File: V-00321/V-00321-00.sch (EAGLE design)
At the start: 3 parts, among them X1 D-SUB9-SAMICE, X2 Lumberg-Lu12MP, X3 LE4MP

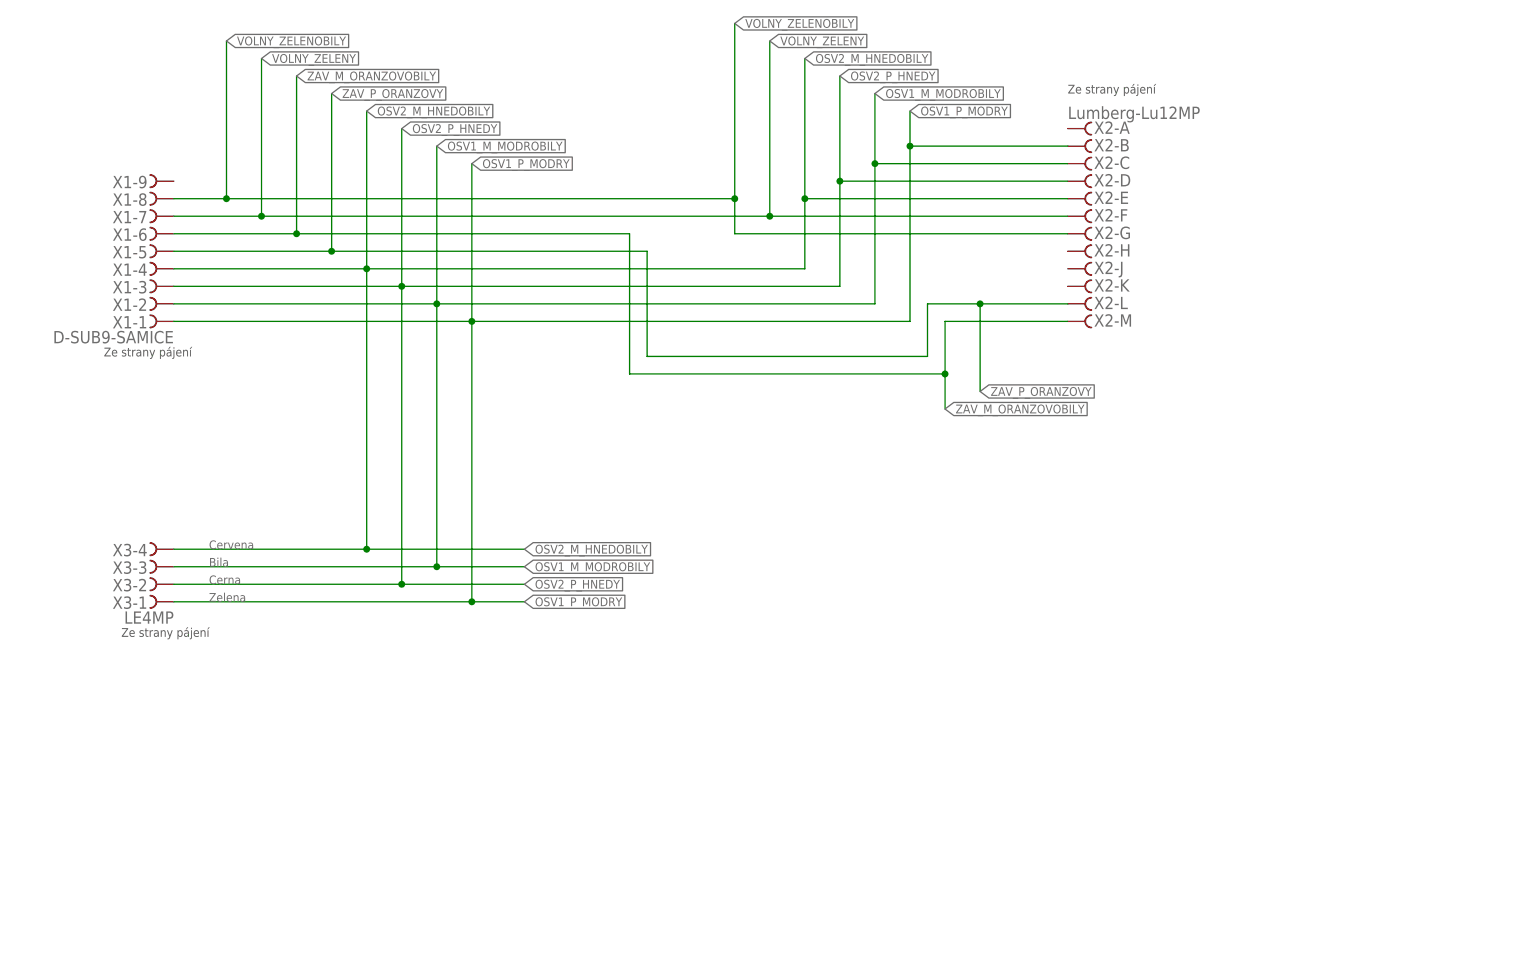
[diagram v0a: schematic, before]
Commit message: Nove kabely a seznam jejich
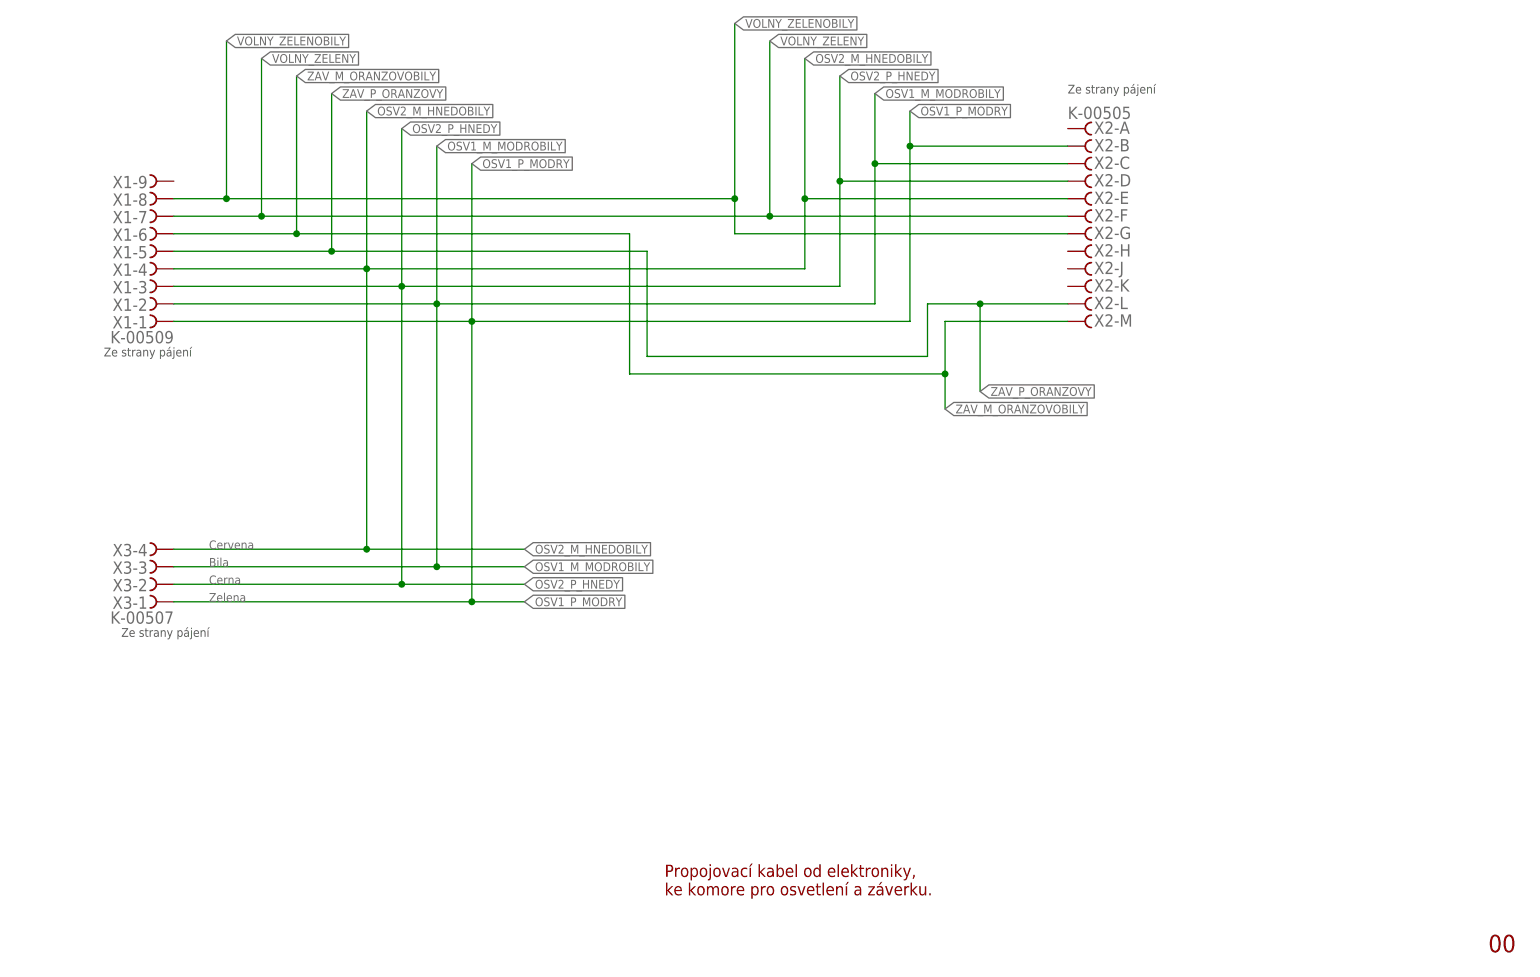
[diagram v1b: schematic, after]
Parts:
- X1: value D-SUB9-SAMICE -> K-00509
- X2: value Lumberg-Lu12MP -> K-00505
- X3: value LE4MP -> K-00507
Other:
- note added: "00"
- note added: "Propojovací kabel od elektroniky, ke komore pro osvetlení a záverku."
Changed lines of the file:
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@@
 <drawing>
 <settings>
-<setting alwaysvectorfont="no"/>
+<setting alwaysvectorfont="yes"/>
 <setting verticaltext="up"/>
 </settings>
@@
 <parts>
 <part name="FRAME1" library="frames" deviceset="A4L-LOC" device=""/>
-<part name="X1" library="con-thomas-betts" deviceset="D-SUB9-" device="H2M09ST" value="D-SUB9-SAMICE"/>
-<part name="X2" library="Kabely" deviceset="LU12MP" device="" value="Lumberg-Lu12MP"/>
-<part name="X3" library="Kabely" deviceset="LE4MP" device=""/>
+<part name="X1" library="con-thomas-betts" deviceset="D-SUB9-" device="H2M09ST" value="K-00509"/>
+<part name="X2" library="Kabely" deviceset="LU12MP" device="" value="K-00505"/>
+<part name="X3" library="Kabely" deviceset="LE4MP" device="" value="K-00507"/>
 </parts>
 <sheets>
@@
 <text x="60.96" y="63.5" size="1.27" layer="95">Cervena</text>
 <text x="48.26" y="50.8" size="1.27" layer="97">Ze strany pájení</text>
+<text x="127" y="17.78" size="1.778" layer="94" align="top-left">Propojovací kabel od elektroniky,
+ke komore pro osvetlení a záverku.</text>
+<text x="246.38" y="7.62" size="2.54" layer="94" align="top-left">00</text>
 </plain>
 <instances>
@@
 </schematic>
 </drawing>
+<compatibility>
+<note version="6.3" minversion="6.2.2" severity="warning">
+Since Version 6.2.2 text objects can contain more than one line,
+which will not be processed correctly with this version.
+</note>
+</compatibility>
 </eagle>
